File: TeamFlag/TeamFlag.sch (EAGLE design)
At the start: 18 parts, among them IC1 ARDUINO_PRO_MICROSMD, Q3 N-CH, Q4 N-CH

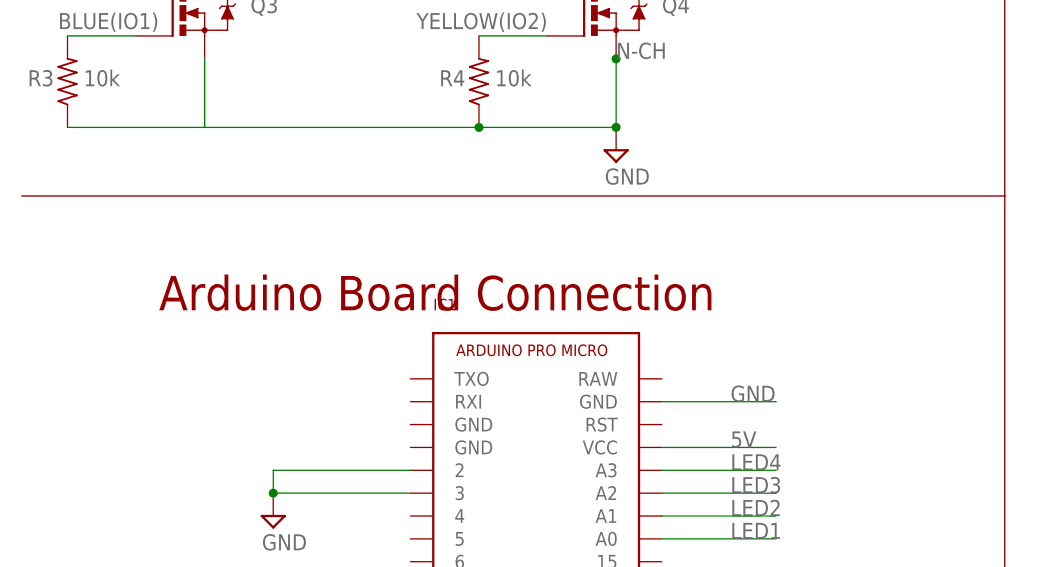
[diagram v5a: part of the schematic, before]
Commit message: Dimension fixes; tkeepout changes
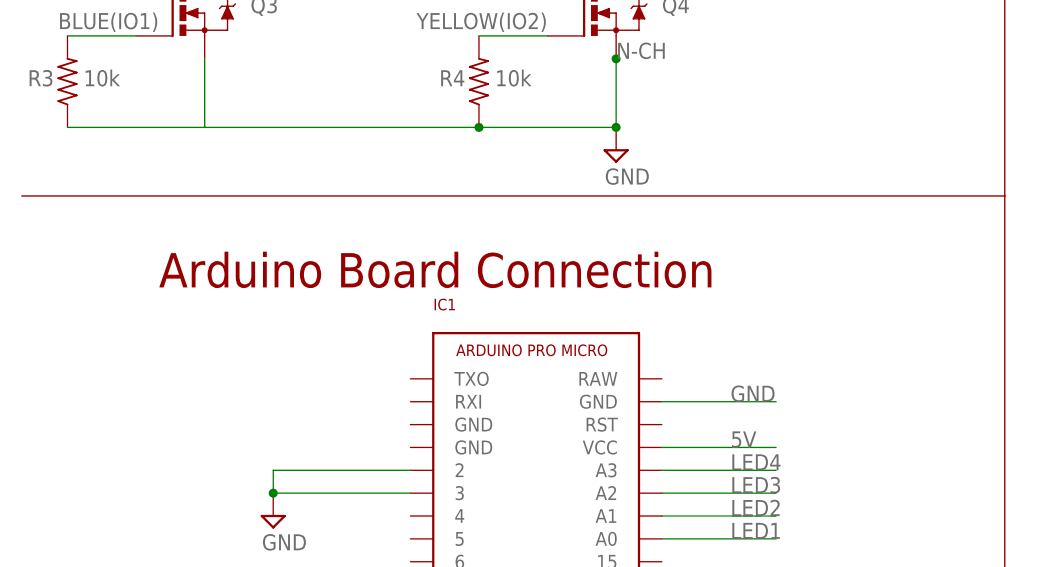
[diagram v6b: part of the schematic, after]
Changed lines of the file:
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@@
 <text x="25.4" y="45.72" size="3.81" layer="94" font="vector">Extra Status LEDs</text>
 <wire x1="109.22" y1="58.42" x2="109.22" y2="0" width="0.1524" layer="94"/>
-<text x="15.24" y="114.3" size="3.81" layer="94" font="vector">Arduino Board Connection</text>
+<text x="15.24" y="116.84" size="3.81" layer="94" font="vector">Arduino Board Connection</text>
 </plain>
 <instances>
